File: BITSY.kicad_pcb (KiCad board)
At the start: 4 copper layers, 102 x 102 mm, 57 parts, among them CON1 AudioJack3_SwitchTR, J1 Barrel_Jack_Switch, J2 Conn_01x06, J3 Conn_01x05, J4 Conn_02x22_Odd_Even, J5 Conn_01x40_Pin, Q1 2N7000, SW1 RESET_SW, U1 MC68HC000FN, U10 ATF22V10C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

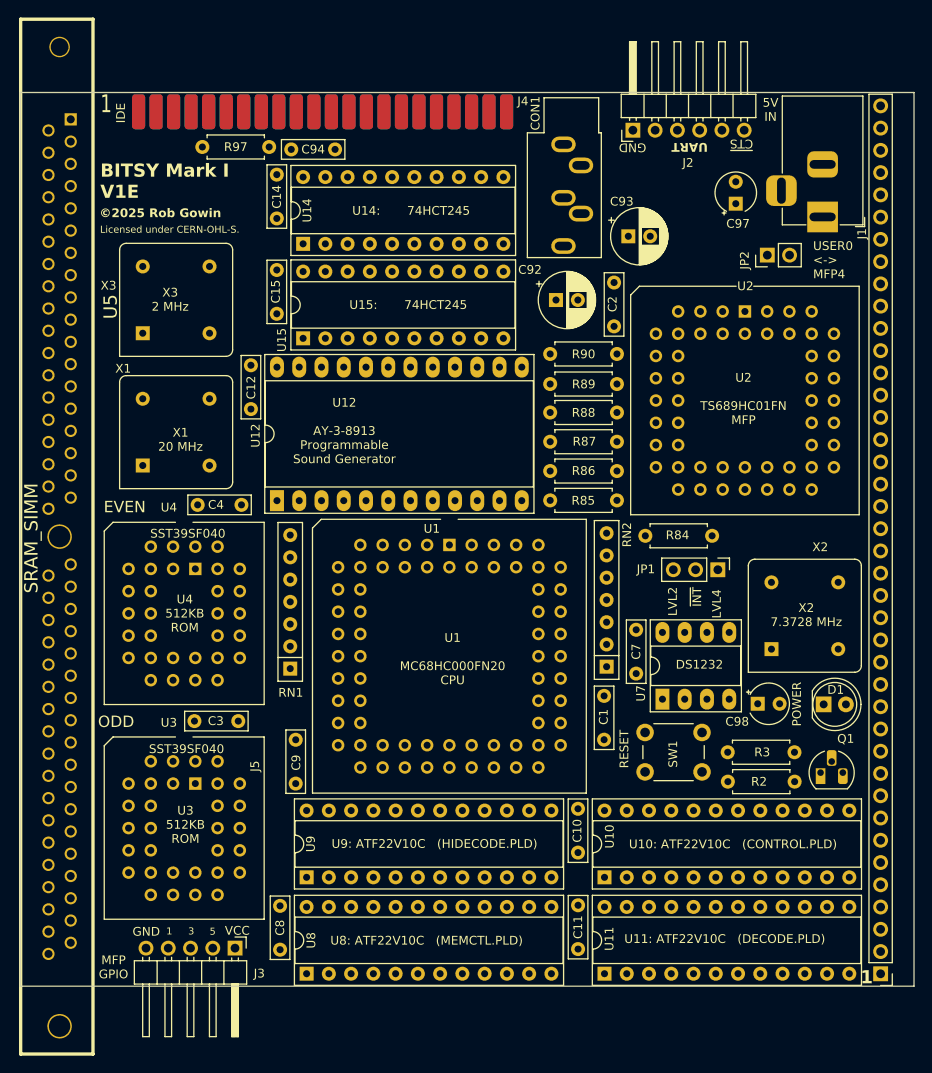
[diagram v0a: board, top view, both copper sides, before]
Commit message: Add routed PCB for V1E.
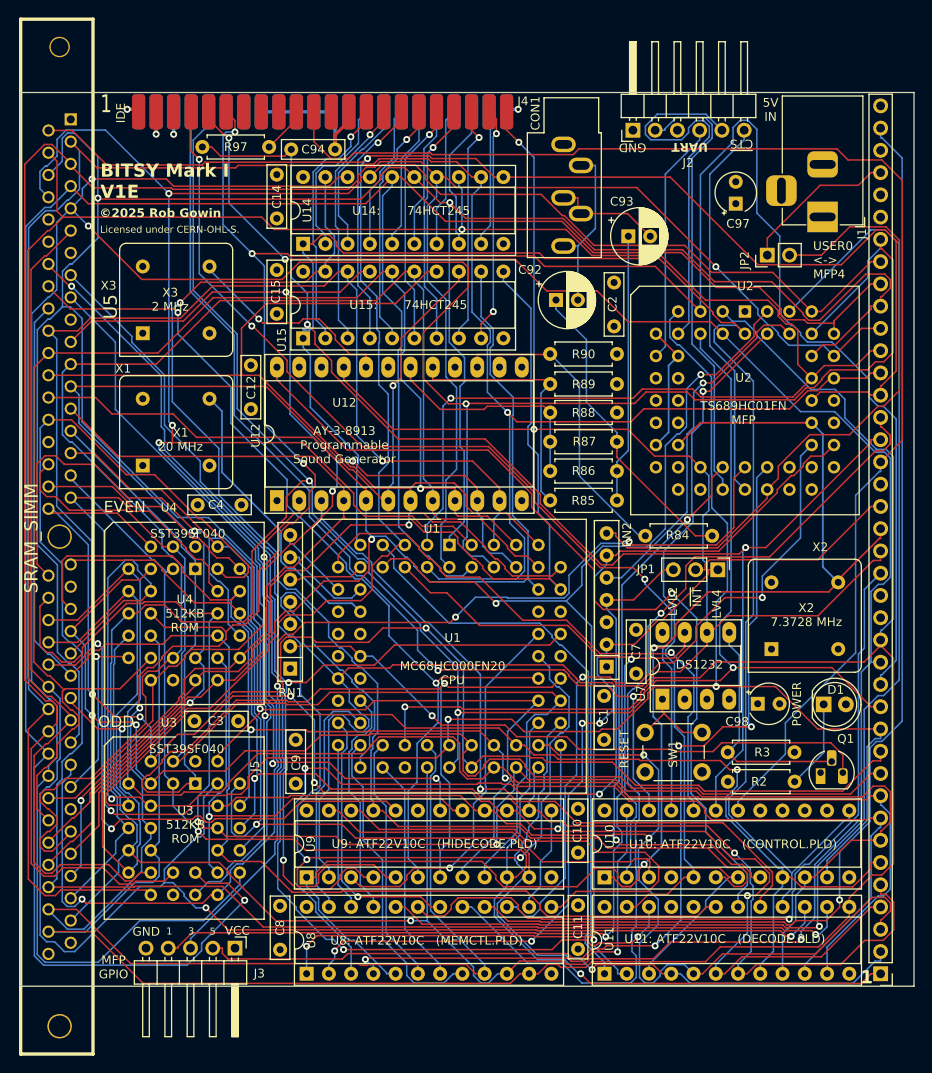
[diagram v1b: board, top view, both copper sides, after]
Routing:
- net /A3: track 0.00 -> 366.1 mm, vias 0 -> 4
- net /D4: track 0.00 -> 324.0 mm, vias 0 -> 2
- net /D7: track 0.00 -> 323.6 mm, vias 0 -> 3
- net /A2: track 0.00 -> 300.8 mm, vias 0 -> 4
- net /A1: track 0.00 -> 287.6 mm, vias 0 -> 1
- net /D5: track 0.00 -> 284.9 mm, vias 0 -> 1
- net /D6: track 0.00 -> 281.9 mm, vias 0 -> 4
- net /D2: track 0.00 -> 274.9 mm, vias 0 -> 2
- net /D0: track 0.00 -> 265.4 mm, vias 0 -> 2
- net /D3: track 0.00 -> 262.4 mm, vias 0 -> 1
- net /D1: track 0.00 -> 259.8 mm, vias 0 -> 1
- net /A4: track 0.00 -> 253.2 mm, vias 0 -> 3
- net /~{RESET}: track 0.00 -> 218.2 mm, vias 0 -> 2
- net /A5: track 0.00 -> 212.0 mm, vias 0 -> 3
- net /A14: track 0.00 -> 203.8 mm, vias 0 -> 3
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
